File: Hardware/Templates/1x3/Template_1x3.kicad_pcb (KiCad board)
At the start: 2 copper layers, 42 x 126 mm, 4 parts

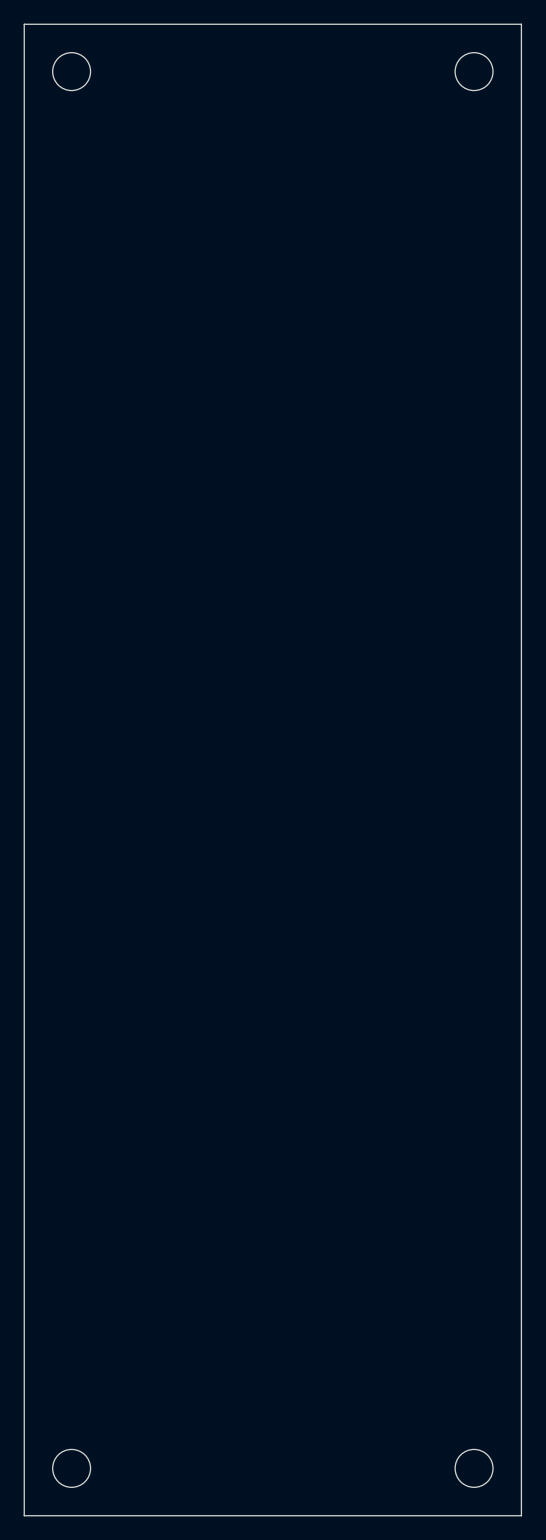
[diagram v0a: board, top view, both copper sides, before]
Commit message: Edited Templates for Hardware
Edited size of templates to fit within containers
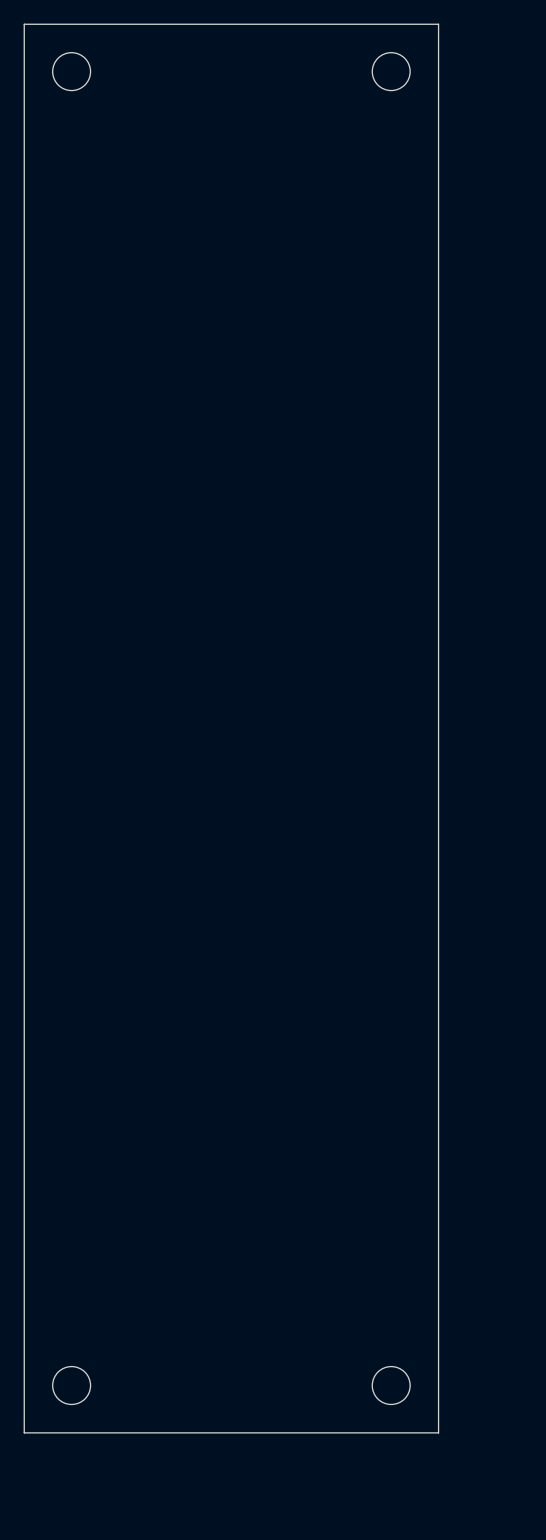
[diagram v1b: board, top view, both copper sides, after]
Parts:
- moved REF** 9.90 mm to (51.0, 135.0)
- moved REF** 7.00 mm to (51.0, 24.0)
- moved REF** 7.00 mm to (24.0, 135.0)
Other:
- board size 42 x 126 mm -> 35 x 119 mm
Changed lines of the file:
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@@
 	(footprint "MountingHole:MountingHole_3.2mm_M3"
 		(layer "F.Cu")
-		(at 58 142)
+		(at 51 135)
 		(descr "Mounting Hole 3.2mm, no annular, M3")
 		(tags "mounting hole 3.2mm no annular m3")
@@
 	(footprint "MountingHole:MountingHole_3.2mm_M3"
 		(layer "F.Cu")
-		(at 58 24)
+		(at 51 24)
 		(descr "Mounting Hole 3.2mm, no annular, M3")
 		(tags "mounting hole 3.2mm no annular m3")
@@
 	(footprint "MountingHole:MountingHole_3.2mm_M3"
 		(layer "F.Cu")
-		(at 24 142)
+		(at 24 135)
 		(descr "Mounting Hole 3.2mm, no annular, M3")
 		(tags "mounting hole 3.2mm no annular m3")
@@
 	(gr_rect
 		(start 20 20)
-		(end 62 146)
+		(end 55 139)
 		(stroke
 			(width 0.1)
